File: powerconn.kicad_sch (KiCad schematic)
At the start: 13 parts, among them CN1 Conn_01x01, CN2 Conn_01x01, CN3 Conn_01x01, K1 HF32FV-16/5-HLTF(590), Q1 MMBT3904

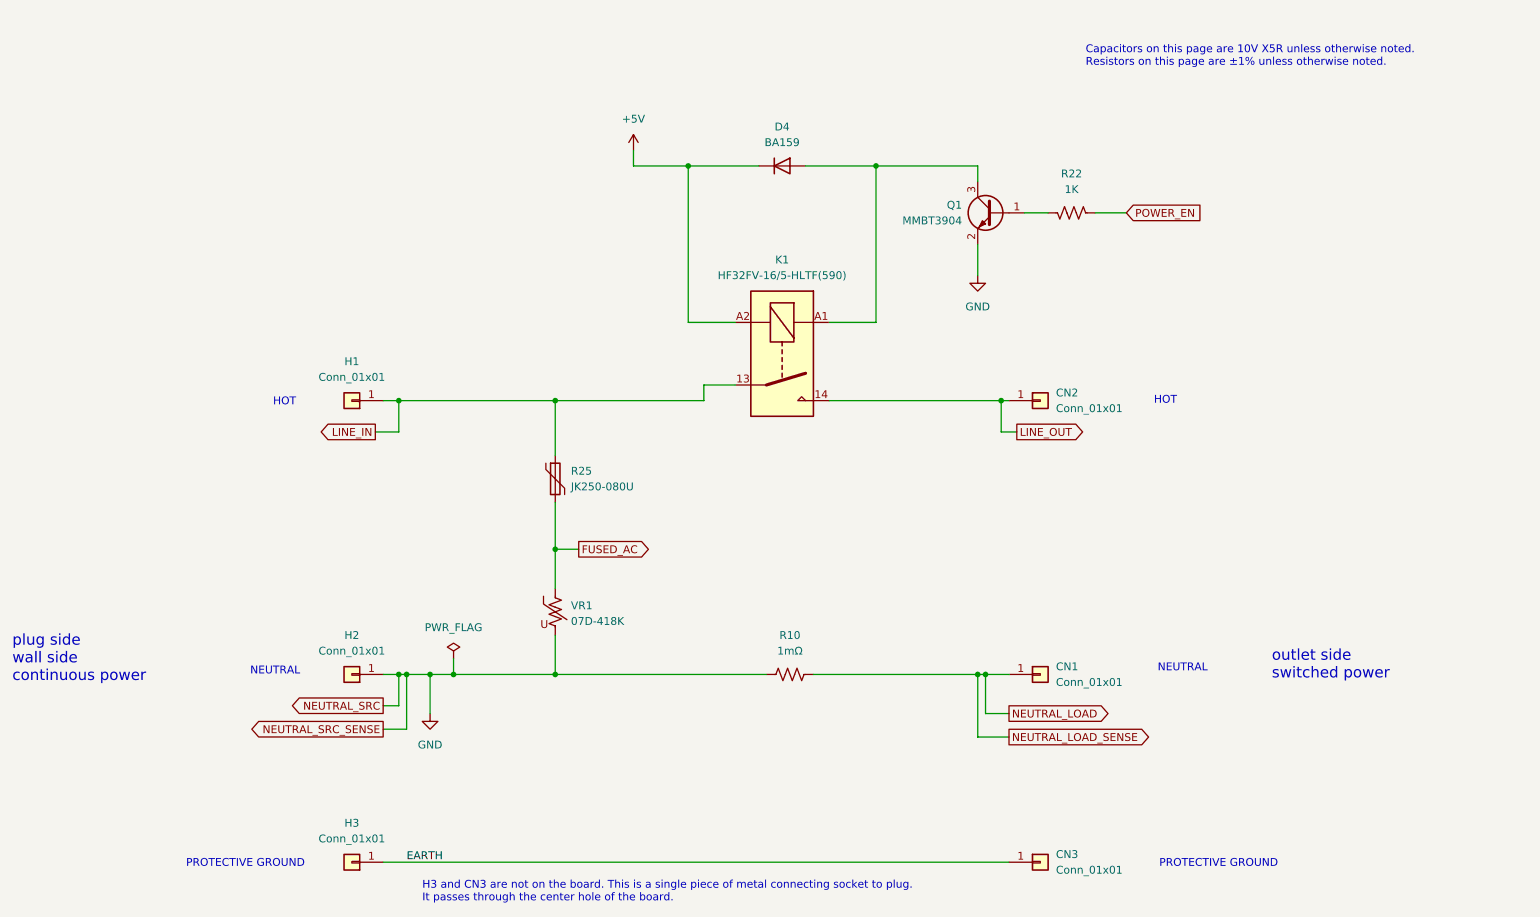
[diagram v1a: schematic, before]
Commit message: Rearranged SMPS circuit. Added a lot of schematic comments. Moved RECT_AC line away from NEUTRAL_SRC (not enough). Updated README greatly. Added pictures. Added PDF schematic.
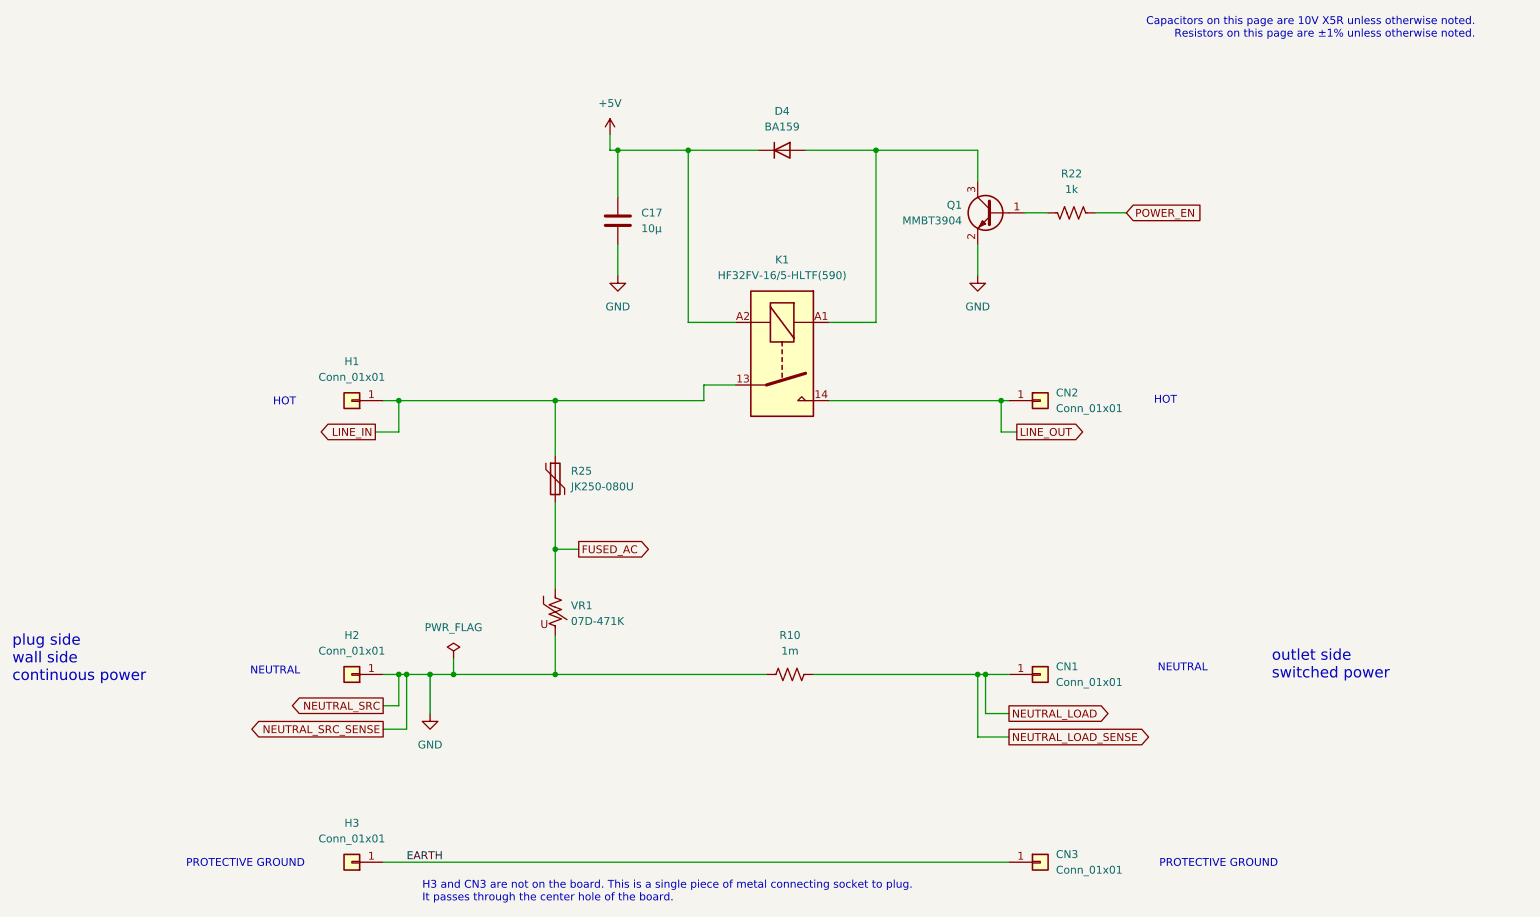
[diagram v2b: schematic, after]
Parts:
- added C17: 10µ, Capacitor_SMD:C_0603_1608Metric, symbol Device:C
- R10: value 1mΩ -> 1m
- R22: value 1K -> 1k
- VR1: value 07D-418K -> 07D-471K
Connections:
- net +5V: now also C17.1
- net GND: now also C17.2
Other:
- moved on the sheet: D4
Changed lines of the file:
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@@
 	(title_block
 		(title "power connections and control")
-		(date "2025-07-28")
+		(date "2025-08-17")
+		(rev "a")
 	)
 	(text "Capacitors on this page are 10V X5R unless otherwise noted.\nResistors on this page are ±1% unless otherwise noted."
 		(exclude_from_sim no)
-		(at 199.136 26.67 0)
-		(effects
-			(font
-				(size 1.27 1.27)
-			)
-			(justify left)
+		(at 262.382 22.098 0)
+		(effects
+			(font
+				(size 1.27 1.27)
+			)
+			(justify right)
 		)
 	)
@@
 	)
 	(junction
-		(at 134.62 44.45)
-		(diameter 0)
-		(color 0 0 0 0)
-	)
-	(junction
 		(at 87.63 127)
 		(diameter 0)
@@
 	)
 	(junction
+		(at 134.62 41.91)
+		(diameter 0)
+		(color 0 0 0 0)
+	)
+	(junction
+		(at 123.19 41.91)
+		(diameter 0)
+		(color 0 0 0 0)
+	)
+	(junction
 		(at 181.61 127)
 		(diameter 0)
@@
 	)
 	(junction
-		(at 165.1 44.45)
+		(at 165.1 41.91)
 		(diameter 0)
 		(color 0 0 0 0)
@@
 	(wire
 		(pts
-			(xy 153.67 44.45) (xy 165.1 44.45)
+			(xy 123.19 41.91) (xy 123.19 49.53)
+		)
+		(stroke
+			(width 0)
+			(type default)
+		)
+	)
+	(wire
+		(pts
+			(xy 153.67 41.91) (xy 165.1 41.91)
 		)
 		(stroke
@@
 	(wire
 		(pts
-			(xy 181.61 44.45) (xy 181.61 46.99)
+			(xy 181.61 41.91) (xy 181.61 46.99)
 		)
 		(stroke
@@
 	(wire
 		(pts
+			(xy 123.19 41.91) (xy 134.62 41.91)
+		)
+		(stroke
+			(width 0)
+			(type default)
+		)
+	)
+	(wire
+		(pts
 			(xy 96.52 124.46) (xy 96.52 127)
 		)
@@
 	(wire
 		(pts
+			(xy 121.92 41.91) (xy 123.19 41.91)
+		)
+		(stroke
+			(width 0)
+			(type default)
+		)
+	)
+	(wire
+		(pts
 			(xy 181.61 137.16) (xy 186.69 137.16)
 		)
@@
 	(wire
 		(pts
-			(xy 181.61 44.45) (xy 165.1 44.45)
+			(xy 181.61 41.91) (xy 165.1 41.91)
 		)
 		(stroke
@@
 	(wire
 		(pts
-			(xy 125.73 41.91) (xy 125.73 44.45)
+			(xy 121.92 39.37) (xy 121.92 41.91)
 		)
 		(stroke
@@
 	(wire
 		(pts
-			(xy 134.62 44.45) (xy 146.05 44.45)
+			(xy 134.62 41.91) (xy 146.05 41.91)
 		)
 		(stroke
@@
 	(wire
 		(pts
+			(xy 134.62 41.91) (xy 134.62 69.85)
+		)
+		(stroke
+			(width 0)
+			(type default)
+		)
+	)
+	(wire
+		(pts
 			(xy 113.03 106.68) (xy 116.84 106.68)
 		)
@@
 	(wire
 		(pts
-			(xy 165.1 44.45) (xy 165.1 69.85)
+			(xy 123.19 57.15) (xy 123.19 62.23)
+		)
+		(stroke
+			(width 0)
+			(type default)
+		)
+	)
+	(wire
+		(pts
+			(xy 165.1 41.91) (xy 165.1 69.85)
 		)
 		(stroke
@@
 	(wire
 		(pts
-			(xy 125.73 44.45) (xy 134.62 44.45)
-		)
-		(stroke
-			(width 0)
-			(type default)
-		)
-	)
-	(wire
-		(pts
 			(xy 113.03 120.65) (xy 113.03 127)
 		)
@@
 		(pts
 			(xy 137.16 80.01) (xy 142.24 80.01)
-		)
-		(stroke
-			(width 0)
-			(type default)
-		)
-	)
-	(wire
-		(pts
-			(xy 134.62 44.45) (xy 134.62 69.85)
 		)
 		(stroke
@@
 	(symbol
 		(lib_id "Diode:BA159")
-		(at 149.86 44.45 0)
+		(at 149.86 41.91 0)
 		(unit 1)
 		(exclude_from_sim no)
@@
 		(fields_autoplaced yes)
 		(property "Reference" "D4"
+			(at 149.86 35.56 0)
+			(effects
+				(font
+					(size 1.27 1.27)
+				)
+			)
+		)
+		(property "Value" "BA159"
 			(at 149.86 38.1 0)
 			(effects
@@
 			)
 		)
-		(property "Value" "BA159"
-			(at 149.86 40.64 0)
-			(effects
-				(font
-					(size 1.27 1.27)
-				)
-			)
-		)
 		(property "Footprint" "Diode_SMD:D_SOD-123F"
-			(at 149.86 48.895 0)
+			(at 149.86 46.355 0)
 			(effects
 				(font
@@
 		)
 		(property "Datasheet" "https://www.vishay.com/docs/88536/ba157.pdf"
-			(at 149.86 44.45 0)
+			(at 149.86 41.91 0)
 			(effects
 				(font
@@
 		)
 		(property "Description" "1000V 1A Fast recovery Rectifier Diode, DO-41"
-			(at 149.86 44.45 0)
+			(at 149.86 41.91 0)
 			(effects
 				(font
@@
 		)
 		(property "Sim.Device" "D"
-			(at 149.86 44.45 0)
+			(at 149.86 41.91 0)
 			(effects
 				(font
@@
 		)
 		(property "Sim.Pins" "1=K 2=A"
-			(at 149.86 44.45 0)
+			(at 149.86 41.91 0)
 			(effects
 				(font
@@
 			)
 		)
-		(property "Value" "1K"
+		(property "Value" "1k"
 			(at 196.85 48.26 90)
 			(effects
@@
 	)
 	(symbol
+		(lib_name "C_3")
+		(lib_id "Device:C")
+		(at 123.19 53.34 0)
+		(unit 1)
+		(exclude_from_sim no)
+		(in_bom yes)
+		(on_board yes)
+		(dnp no)
+		(fields_autoplaced yes)
+		(property "Reference" "C17"
+			(at 127 52.0699 0)
+			(effects
+				(font
+					(size 1.27 1.27)
+				)
+				(justify left)
+			)
+		)
+		(property "Value" "10µ"
+			(at 127 54.6099 0)
+			(effects
+				(font
+					(size 1.27 1.27)
+				)
+				(justify left)
+			)
+		)
+		(property "Footprint" "Capacitor_SMD:C_0603_1608Metric"
+			(at 124.1552 57.15 0)
+			(effects
+				(font
+					(size 1.27 1.27)
+				)
+				(hide yes)
+			)
+		)
+		(property "Datasheet" "~"
+			(at 123.19 53.34 0)
+			(effects
+				(font
+					(size 1.27 1.27)
+				)
+				(hide yes)
+			)
+		)
+		(property "Description" "Unpolarized capacitor"
+			(at 123.19 53.34 0)
+			(effects
+				(font
+					(size 1.27 1.27)
+				)
+				(hide yes)
+			)
+		)
+		(pin "1"
+		)
+		(pin "2"
+		)
+		(instances
+			(project "smart-outlet-m-reverse"
+				(path "/0b789f5a-74d1-4f81-bd1f-7ac838c6392e/0d0b8180-7ba4-4dc9-99b6-4281183d15f0"
+					(reference "C17")
+					(unit 1)
+				)
+			)
+		)
+	)
+	(symbol
 		(lib_id "Device:R_US")
 		(at 151.13 127 90)
@@
 			)
 		)
-		(property "Value" "1mΩ"
+		(property "Value" "1m"
 			(at 151.13 123.19 90)
 			(effects
@@
 	(symbol
 		(lib_id "power:+5V")
-		(at 125.73 41.91 0)
+		(at 121.92 39.37 0)
 		(mirror y)
 		(unit 1)
@@
 		(fields_autoplaced yes)
 		(property "Reference" "#PWR021"
-			(at 125.73 45.72 0)
+			(at 121.92 43.18 0)
 			(effects
 				(font
@@
 		)
 		(property "Value" "+5V"
-			(at 125.73 36.83 0)
+			(at 121.92 34.29 0)
 			(effects
 				(font
@@
 		)
 		(property "Footprint" ""
-			(at 125.73 41.91 0)
+			(at 121.92 39.37 0)
 			(effects
 				(font
@@
 		)
 		(property "Datasheet" ""
-			(at 125.73 41.91 0)
+			(at 121.92 39.37 0)
 			(effects
 				(font
@@
 		)
 		(property "Description" "Power symbol creates a global label with name \"+5V\""
-			(at 125.73 41.91 0)
+			(at 121.92 39.37 0)
 			(effects
 				(font
@@
 			)
 		)
-		(property "Value" "07D-418K"
+		(property "Value" "07D-471K"
 			(at 115.57 118.3667 0)
 			(effects
@@
 			)
 		)
-		(property "Datasheet" "~"
+		(property "Datasheet" "https://www.lcsc.com/datasheet/C273550.pdf"
 			(at 113.03 116.84 0)
 			(effects
@@
 					(unit 1)
 				)
+			)
+		)
+	)
+	(symbol
+		(lib_id "power:GND")
+		(at 123.19 62.23 0)
+		(mirror y)
+		(unit 1)
+		(exclude_from_sim no)
+		(in_bom yes)
+		(on_board yes)
+		(dnp no)
+		(fields_autoplaced yes)
+		(property "Reference" "#PWR026"
+			(at 123.19 68.58 0)
+			(effects
+				(font
+					(size 1.27 1.27)
+				)
+				(hide yes)
+			)
+		)
+		(property "Value" "GND"
+			(at 123.19 67.31 0)
+			(effects
+				(font
+					(size 1.27 1.27)
+				)
+			)
+		)
+		(property "Footprint" ""
+			(at 123.19 62.23 0)
+			(effects
+				(font
+					(size 1.27 1.27)
+				)
+				(hide yes)
+			)
+		)
+		(property "Datasheet" ""
+			(at 123.19 62.23 0)
+			(effects
+				(font
+					(size 1.27 1.27)
+				)
+				(hide yes)
+			)
+		)
+		(property "Description" "Power symbol creates a global label with name \"GND\" , ground"
+			(at 123.19 62.23 0)
+			(effects
+				(font
+					(size 1.27 1.27)
+				)
+				(hide yes)
+			)
+		)
+		(pin "1"
+		)
+		(instances
+			(project "smart-outlet-m-reverse"
+				(path "/0b789f5a-74d1-4f81-bd1f-7ac838c6392e/0d0b8180-7ba4-4dc9-99b6-4281183d15f0"
+					(reference "#PWR026")
+					(unit 1)
+				)
